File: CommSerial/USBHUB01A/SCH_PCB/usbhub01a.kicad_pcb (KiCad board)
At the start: 4 copper layers, 80.8 x 80.8 mm, 140 parts, among them CON1 BARREL_JACK, J1 JUMP_2x1, J12 JUMP_5X2, J13 USB3_A, J14 USB3_B, J15 USB3_A, J16 USB3_A, J17 USB3_A, J18 JUMP_3X2, J2 JUMP_6X2, M1 HOLE, M2 HOLE, M3 HOLE, M4 HOLE, SW1 SPST, U1 CAT24C04YI-GT3OSCT-ND, U2 TUSB8041IPAPRQ1, U3 TPS7A4533KTTR, U4 TPS74801RGWR, U5 TPS2001CDGN, U6 TPS2001CDGN, U7 TPS2001CDGN, U8 TPS2001CDGN, Y1 24MHz

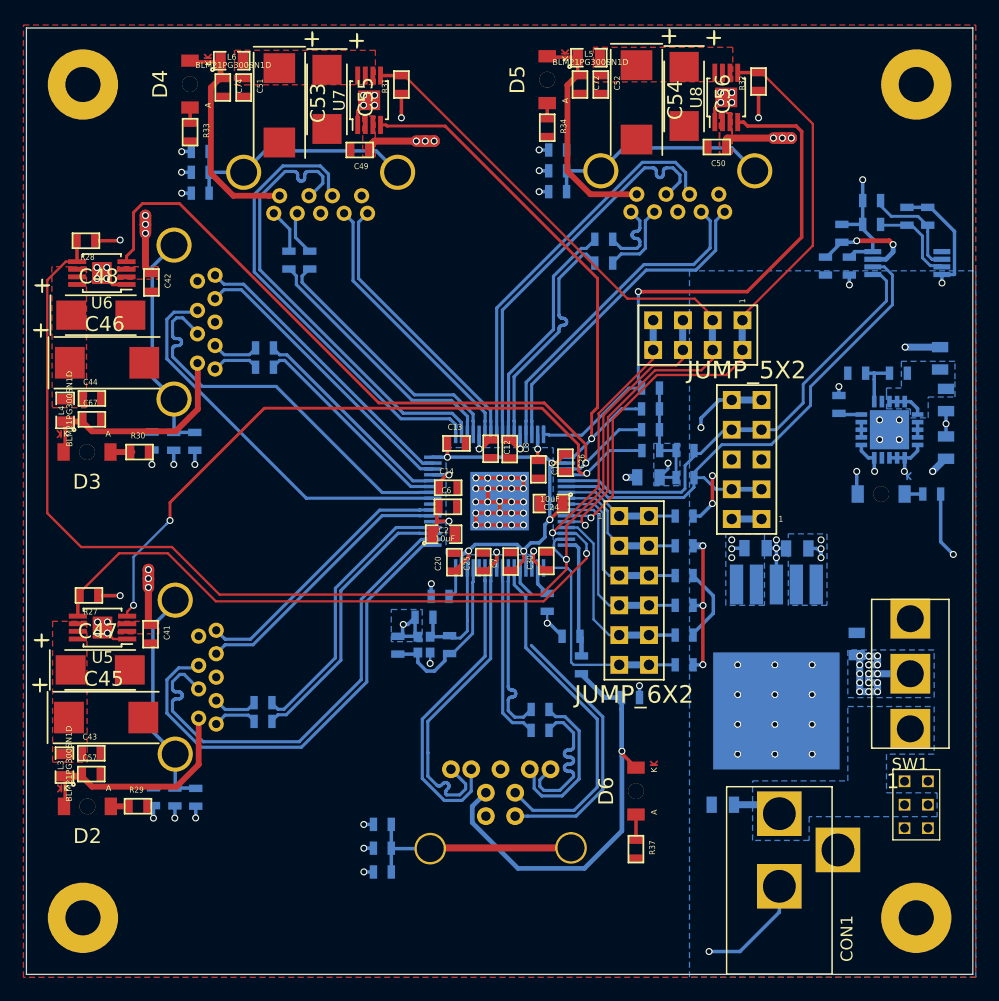
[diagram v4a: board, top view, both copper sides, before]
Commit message: Presunute pullup rezistory USB PowerOn
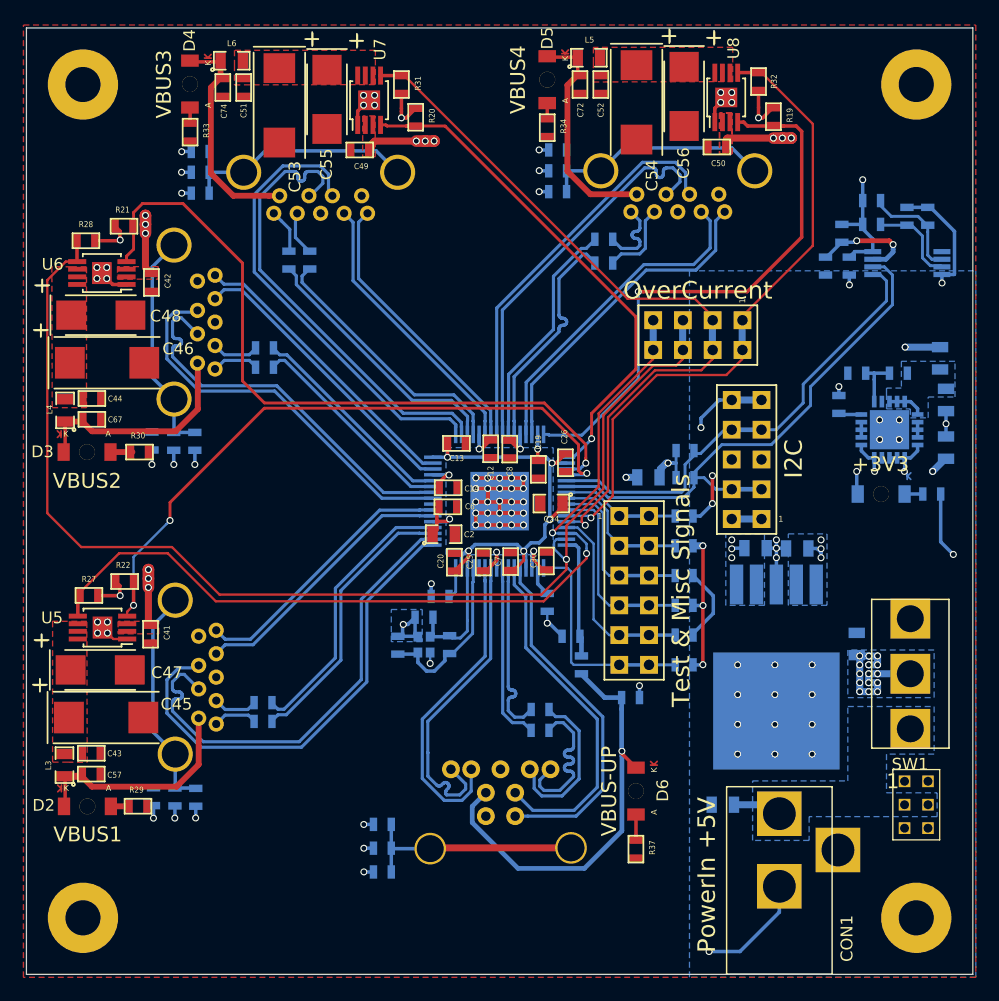
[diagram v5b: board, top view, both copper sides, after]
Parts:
- CON1: value BARREL_JACK -> PowerIn +5V
- D1: value LED -> +3V3
- D2: value LED -> VBUS1
- D3: value LED -> VBUS2
- D4: value LED -> VBUS3
- D5: value LED -> VBUS4
- D6: value GREEN -> VBUS-UP
- J1: value JUMP_2x1 -> OverCurrent
- J12: value JUMP_5X2 -> I2C
- J2: value JUMP_6X2 -> Test & Misc Signals
- R19, R20, R21, R22: moved to F.Cu
- moved R21 48.2 mm to (115.3, 78.1), turned to 0 degrees
- moved R22 46.3 mm to (115.3, 108.5), turned to 0 degrees
- moved R20 32.0 mm to (140.2, 68.8), turned to 270 degrees
- moved R19 25.4 mm to (170.7, 68.8), turned to 270 degrees
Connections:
- U1 pad 1: (no net) -> Net-(U1-Pad1)
- U2 pad 28: (no net) -> Net-(U2-Pad28)
- U2 pad 40: (no net) -> Net-(U2-Pad40)
- U4 pad 17: (no net) -> Net-(U4-Pad17)
- U4 pad 9: (no net) -> Net-(U4-Pad9)
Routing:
- net /USB_DM_UP+: track 26.4 -> 30.8 mm
- net /PWRON1_BATEN1: track 61.0 -> 57.6 mm
- net /PWRON3_BATEN3: track 46.0 -> 44.2 mm
- net /USB_SSTXM_DN2-: track 19.3 -> 17.8 mm
- net +3V3: track 224.7 -> 223.3 mm
- net /USB_SSTXM_DN2+: track 19.1 -> 17.7 mm
- net /USB_SSRXM_DN3+: track 25.2 -> 24.3 mm
- net /USB_SSRXM_DN3-: track 24.7 -> 23.9 mm
- net /USB_SSRXM_DN2+: track 25.4 -> 24.6 mm
- net /USB_DM_DN3+: track 39.8 -> 39.0 mm
- net /USB_DM_DN3-: track 39.8 -> 39.0 mm
- net /USB_SSRXM_DN2-: track 25.4 -> 24.6 mm
- net /PWRON4_BATEN4: track 50.5 -> 49.9 mm
- net /PWRON2_BATEN2: track 61.3 -> 61.8 mm
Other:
- net class Default: clearance 0.2 -> 0.199
- rule trace_clearance: 0.2 -> 0.199

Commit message: Dokončené popisky
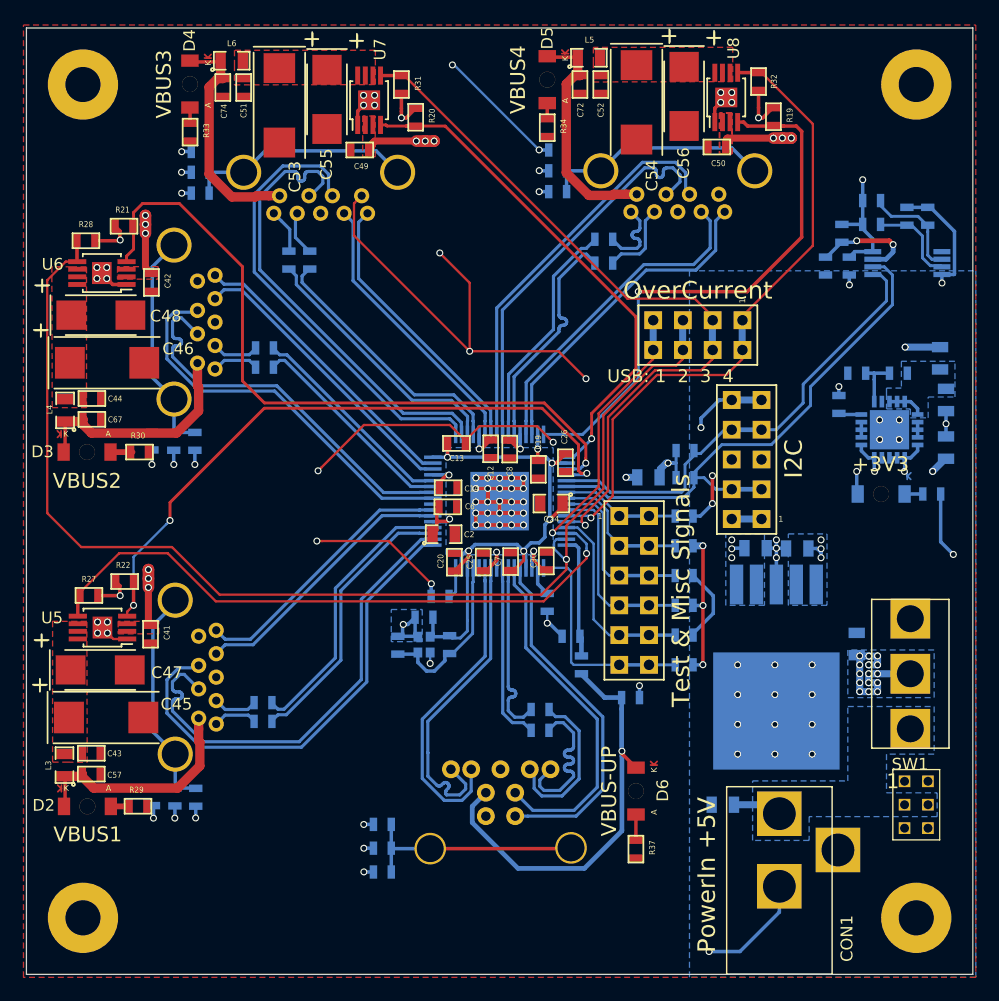
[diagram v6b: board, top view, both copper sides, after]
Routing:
- net GND: track 160.3 -> 243.9 mm, vias 89 -> 96
- net /VBUS2: track 19.4 -> 20.1 mm
- net /VBUS3: track 19.9 -> 20.6 mm
- net /VBUS4: track 19.7 -> 20.4 mm
- net /VBUS1: track 19.5 -> 20.0 mm
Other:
- net class Default: clearance 0.199 -> 0.2
- rule trace_clearance: 0.199 -> 0.2
- board text added: "USB: 1 2 3 4"

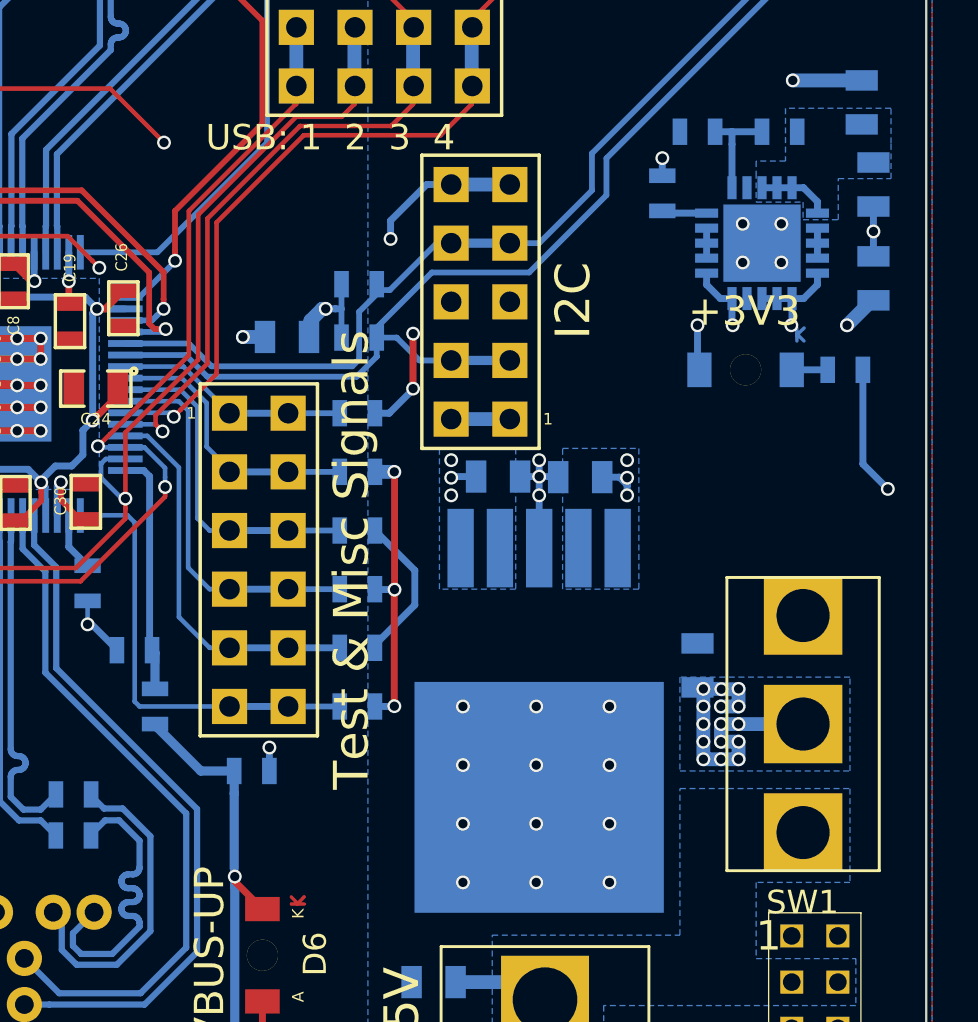
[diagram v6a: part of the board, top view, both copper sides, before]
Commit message: Doplněné popisky
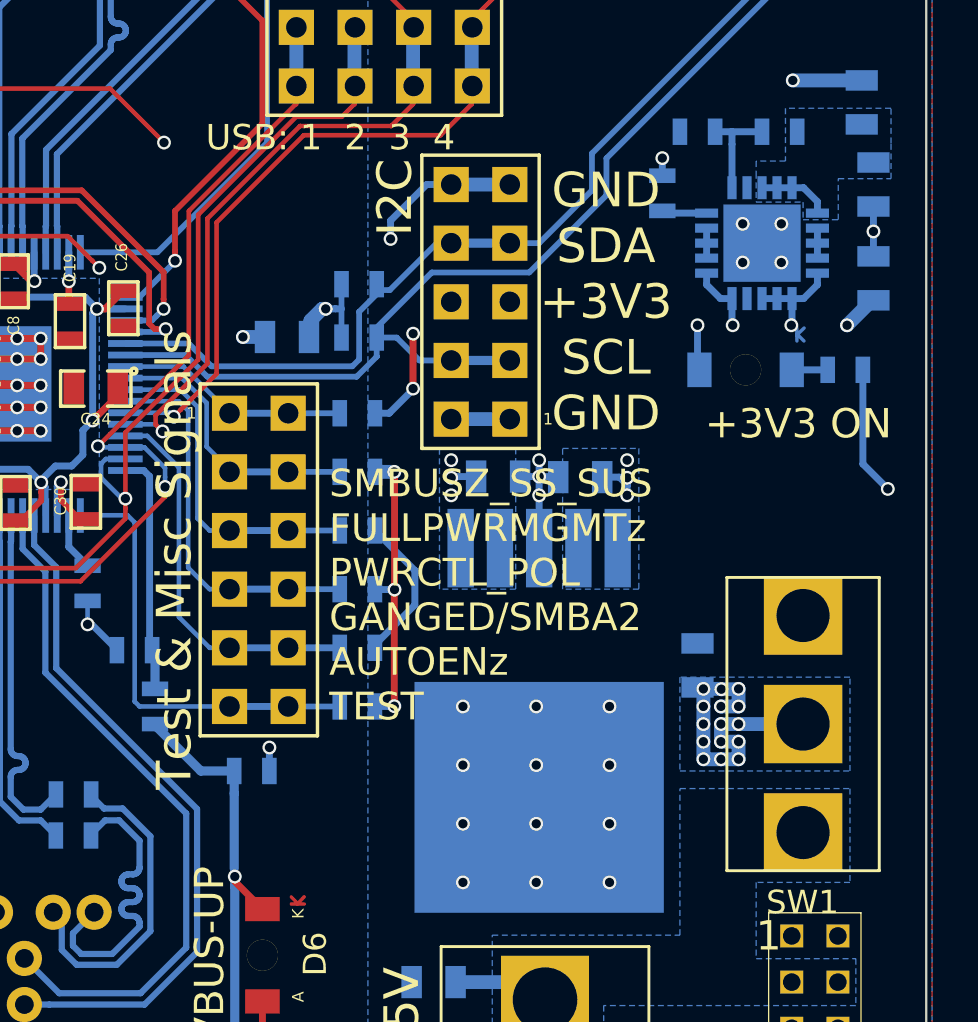
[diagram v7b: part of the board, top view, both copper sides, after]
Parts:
- D1: value +3V3 -> +3V3 ON
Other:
- board text added: "GND SDA +3V3 SCL GND"
- board text added: "SMBUSZ_SS_SUS FULLPWRMGMTz PWRCTL_POL GANGED/SMBA2 AUTOENz TEST"
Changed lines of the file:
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@@
   (general
     (thickness 1.6)
-    (drawings 5)
+    (drawings 7)
     (tracks 1679)
     (zones 0)
@@
   (page A4)
   (layers
-    (0 F.Cu signal)
-    (1 In1.Cu signal)
+    (0 F.Cu signal hide)
+    (1 In1.Cu signal hide)
     (2 In2.Cu signal hide)
-    (31 B.Cu signal)
+    (31 B.Cu signal hide)
     (32 B.Adhes user)
     (33 F.Adhes user)
@@
   )
   (setup
-    (last_trace_width 0.8)
+    (last_trace_width 0.2)
     (user_trace_width 0.2)
     (user_trace_width 0.25)
@@
       (effects (font (size 1 1) (thickness 0.15)) (justify mirror))
     )
-    (fp_text value +3V3 (at -0.0508 -2.54) (layer F.SilkS)
+    (fp_text value "+3V3 ON" (at 2.286 2.3368) (layer F.SilkS)
       (effects (font (thickness 0.15)))
     )
@@
       (effects (font (size 1.5 1.5) (thickness 0.15)))
     )
-    (fp_text value I2C (at -4.0132 0.0508 270) (layer F.SilkS)
+    (fp_text value I2C (at 3.7084 4.5212 90) (layer F.SilkS)
       (effects (font (size 1.5 1.5) (thickness 0.15)))
     )
@@
       (effects (font (size 1.5 1.5) (thickness 0.15)))
     )
-    (fp_text value "Test & Misc Signals" (at 4.0132 0 90) (layer F.SilkS)
+    (fp_text value "Test & Misc Signals" (at -3.6576 0 90) (layer F.SilkS)
       (effects (font (size 1.5 1.5) (thickness 0.15)))
     )
@@
     )
   )
+  (gr_text "SMBUSZ_SS_SUS\nFULLPWRMGMTz\nPWRCTL_POL\nGANGED/SMBA2\nAUTOENz\nTEST " (at 161.8488 110.744) (layer F.SilkS)
+    (effects (font (size 1.2 1.2) (thickness 0.15)) (justify left))
+  )
+  (gr_text "GND\nSDA\n+3V3\nSCL\nGND" (at 173.8376 98.044) (layer F.SilkS)
+    (effects (font (size 1.5 1.5) (thickness 0.15)))
+  )
   (gr_text "USB: 1  2  3  4" (at 161.8996 90.932) (layer F.SilkS)

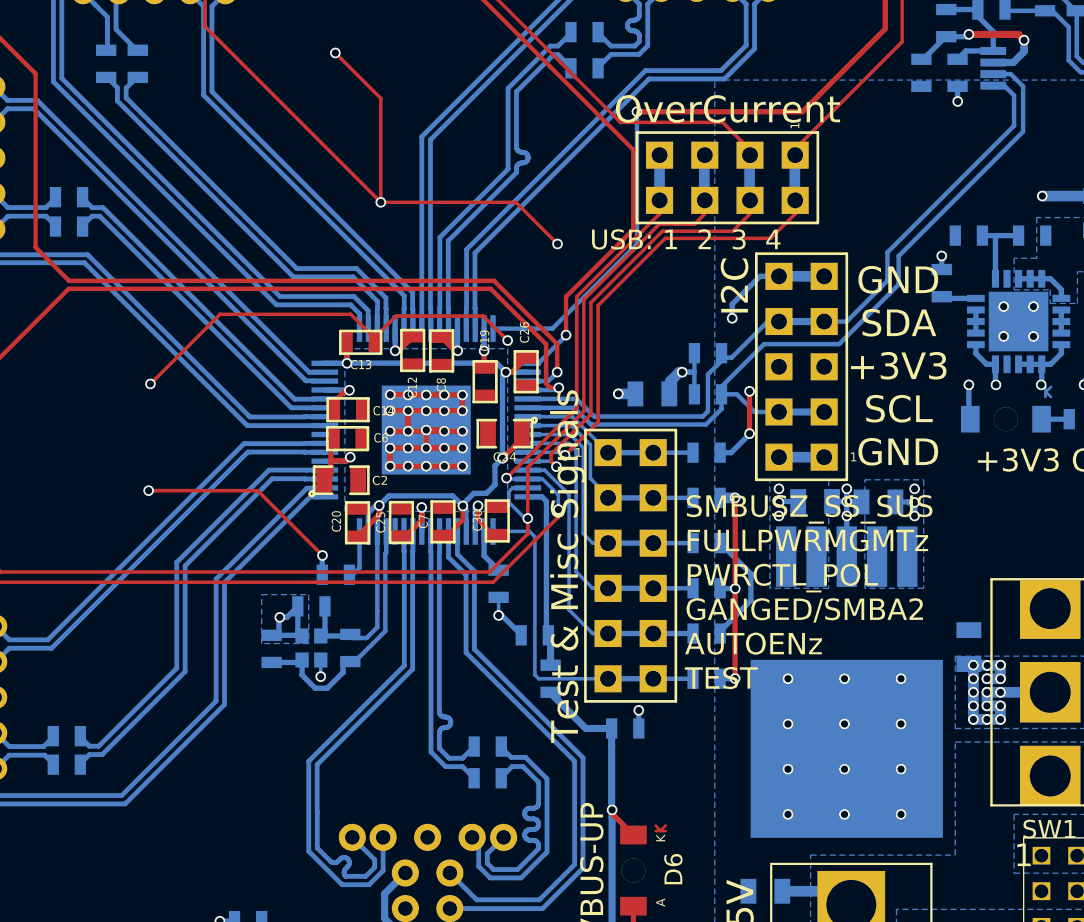
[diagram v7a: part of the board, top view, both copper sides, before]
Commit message: Dokončené popisky
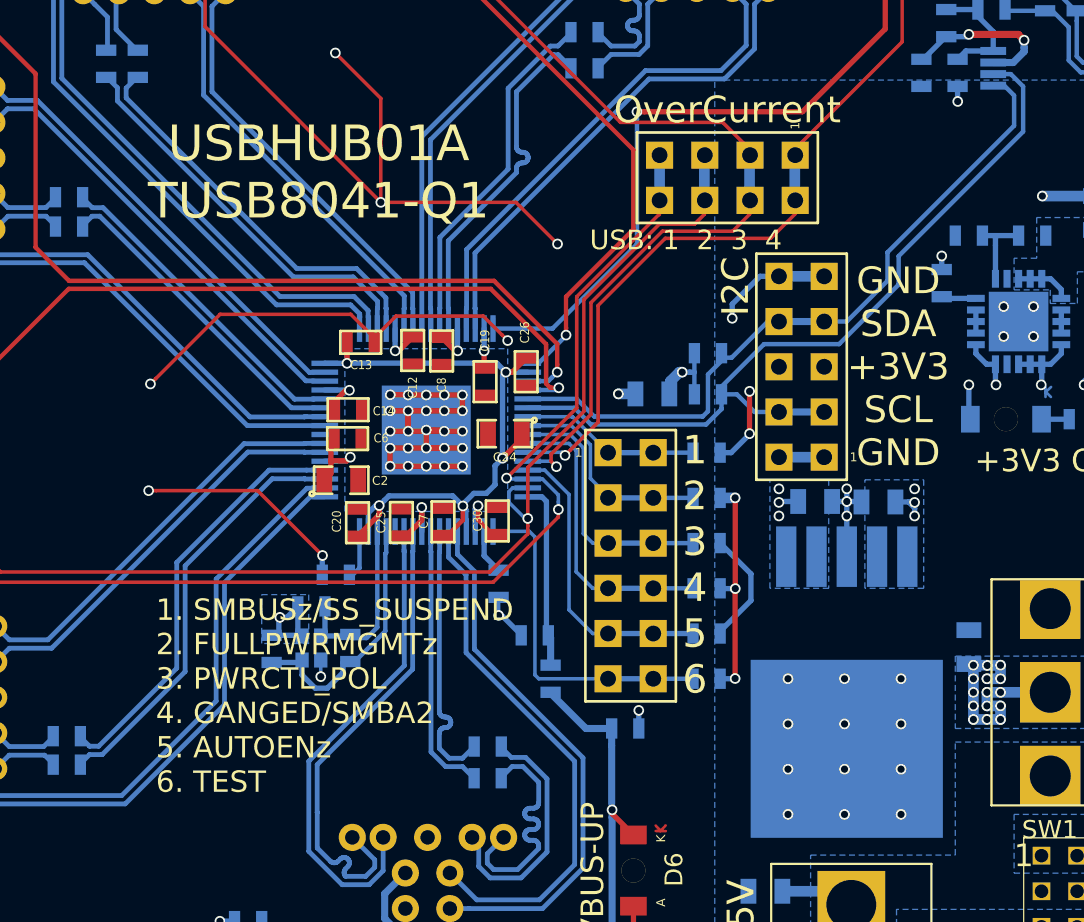
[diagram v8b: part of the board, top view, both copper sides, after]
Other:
- board text added: "1 2 3 4 5 6"
- board text added: "1. SMBUSz/SS_SUSPEND 2. FULLPWRMGMTz 3. PWRCTL_POL 4. GANGED/SMBA2 5. AUTOENz 6. TEST"
- board text added: "USBHUB01A TUSB8041-Q1"
- board text removed: "SMBUSZ_SS_SUS FULLPWRMGMTz PWRCTL_POL GANGED/SMBA2 AUTOENz TEST"
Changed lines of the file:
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@@
   (general
     (thickness 1.6)
-    (drawings 7)
+    (drawings 9)
     (tracks 1679)
     (zones 0)
@@
       (effects (font (size 1.5 1.5) (thickness 0.15)))
     )
-    (fp_text value "Test & Misc Signals" (at -3.6576 0 90) (layer F.SilkS)
+    (fp_text value "Test & Misc Signals" (at -3.6576 0 90) (layer F.SilkS) hide
       (effects (font (size 1.5 1.5) (thickness 0.15)))
     )
@@
     )
   )
-  (gr_text "SMBUSZ_SS_SUS\nFULLPWRMGMTz\nPWRCTL_POL\nGANGED/SMBA2\nAUTOENz\nTEST " (at 161.8488 110.744) (layer F.SilkS)
+  (gr_text "USBHUB01A\nTUSB8041-Q1" (at 141.2748 87.122) (layer F.SilkS)
+    (effects (font (size 2 2) (thickness 0.3)))
+  )
+  (gr_text "1\n2\n3\n4\n5\n6" (at 162.4076 109.1692) (layer F.SilkS)
+    (effects (font (size 1.6 1.6) (thickness 0.15)))
+  )
+  (gr_text "1. SMBUSz/SS_SUSPEND\n2. FULLPWRMGMTz\n3. PWRCTL_POL\n4. GANGED/SMBA2\n5. AUTOENz\n6. TEST " (at 132.1308 116.5352) (layer F.SilkS)
     (effects (font (size 1.2 1.2) (thickness 0.15)) (justify left))
   )
